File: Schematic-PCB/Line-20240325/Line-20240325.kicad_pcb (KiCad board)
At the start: 2 copper layers, 195 x 168 mm, 132 parts, among them J1 Conn_01x02_Pin, J2 Conn_01x04_Pin, J4 Conn_01x06_Pin, SW1 SW_Push, U34 ATmega2560-16A

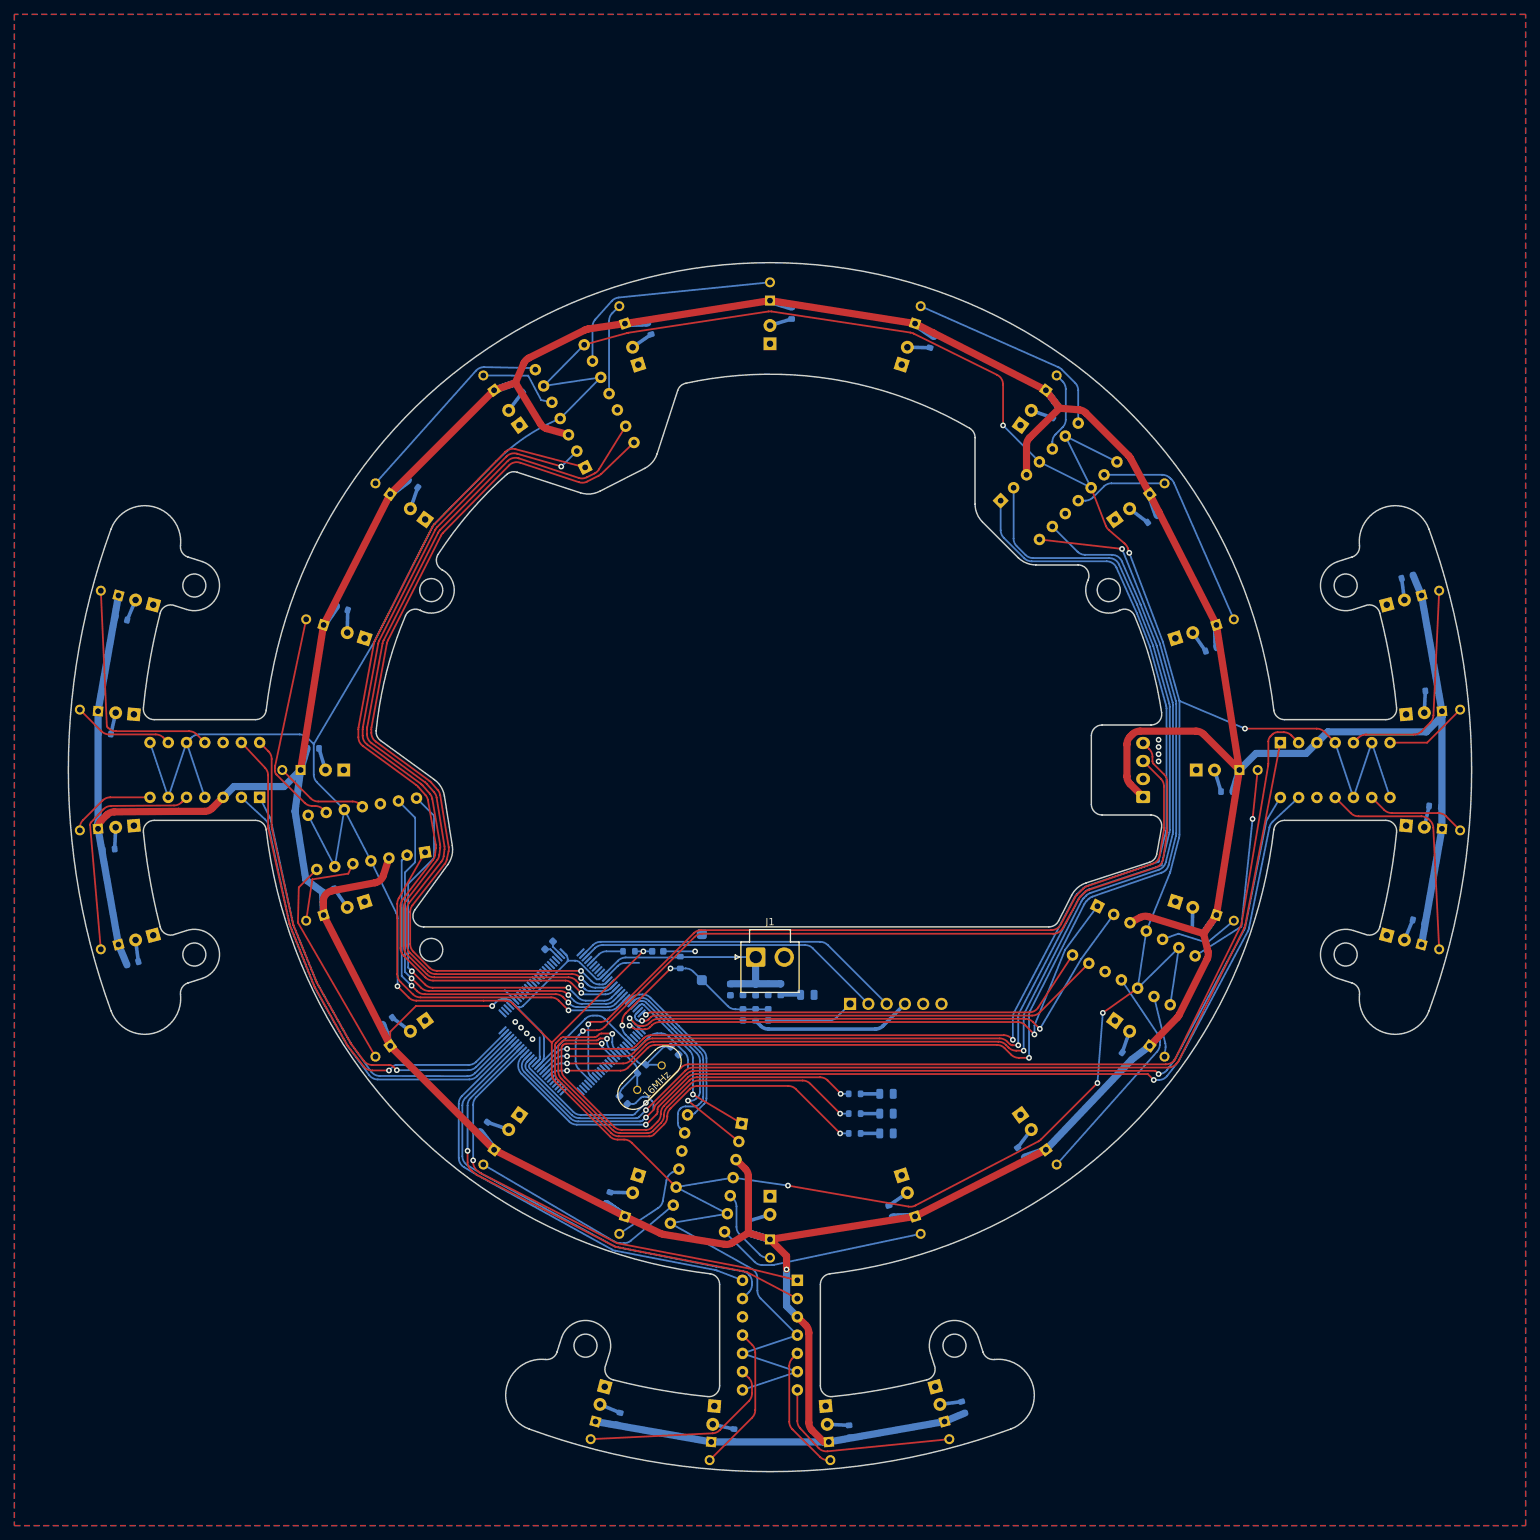
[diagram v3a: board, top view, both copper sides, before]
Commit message: ラインセンサ基板DR完了！！！！
発注用ファイルも出力完了、発注へ進みますー
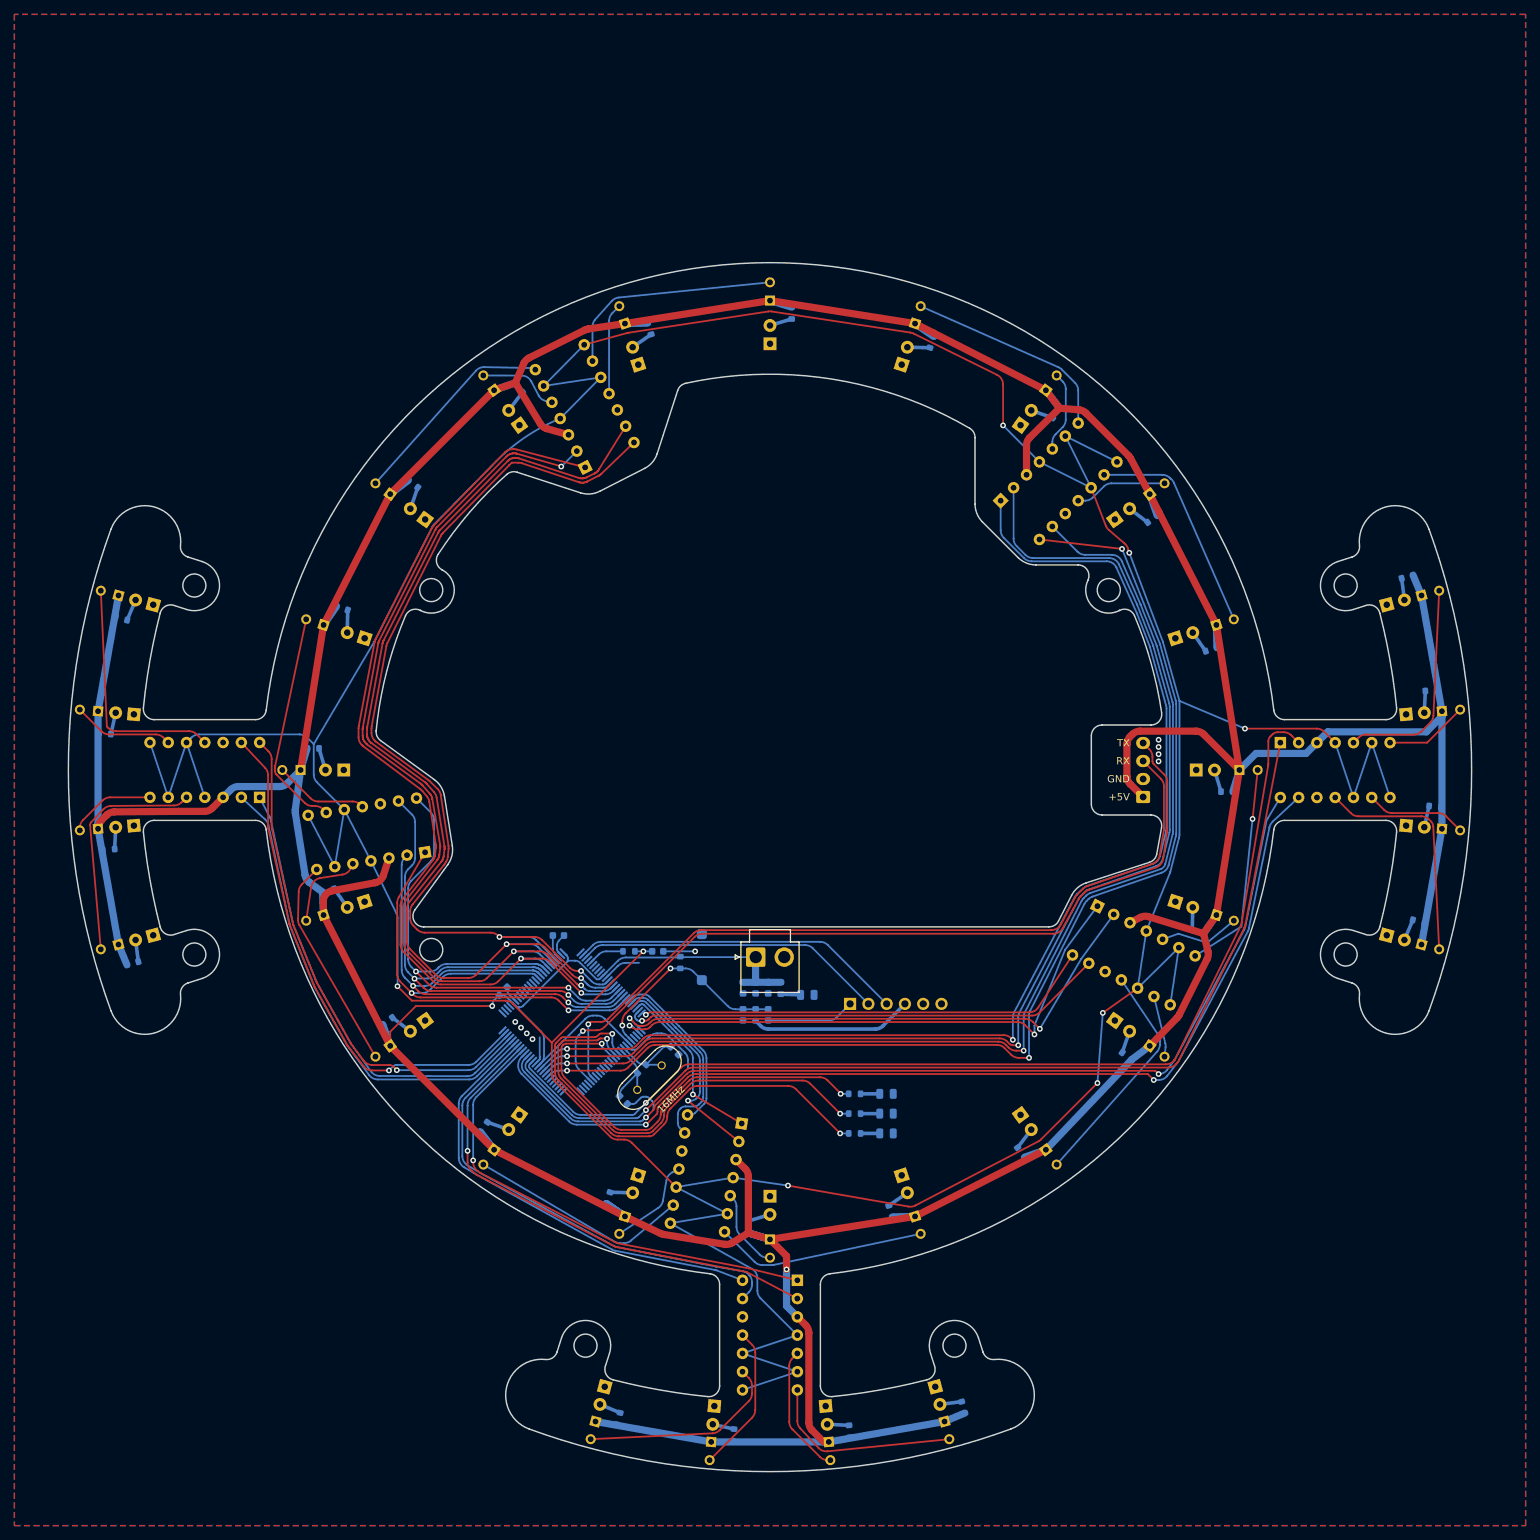
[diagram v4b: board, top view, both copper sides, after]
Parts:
- moved C4 31.6 mm to (-37.1, 30.7), turned to 45 degrees
- moved C6 1.89 mm to (-29.4, 23.0), turned to 0 degrees
- moved C2 0.25 mm to (-2.00, 30.3)
- moved C3 0.22 mm to (-3.75, 30.3)
- moved C1 0.22 mm to (-0.25, 30.3)
- moved R34 0.17 mm to (1.50, 30.3)
- renumbered C8 to 22pF, C7 to 22pF, 16MHz to Y1
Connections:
- U34 pad 90: unconnected-(U34-PF7/ADC7-Pad90) -> line08
- U34 pad 91: unconnected-(U34-PF6/ADC6-Pad91) -> line07
- U34 pad 92: unconnected-(U34-PF5/ADC5-Pad92) -> line06
- U34 pad 93: unconnected-(U34-PF4/ADC4-Pad93) -> line05
- U34 pad 94: unconnected-(U34-PF3/ADC3-Pad94) -> line04
- U34 pad 95: unconnected-(U34-PF2/ADC2-Pad95) -> line03
- U34 pad 96: unconnected-(U34-PF1/ADC1-Pad96) -> line02
- U34 pad 97: unconnected-(U34-PF0/ADC0-Pad97) -> line01
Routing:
- net line08: track 52.6 -> 71.7 mm, vias 1 -> 2
- net line07: track 50.2 -> 68.6 mm
- net line06: track 57.5 -> 75.7 mm
- net line05: track 57.6 -> 75.6 mm
- net line02: track 131.3 -> 142.3 mm, vias 1 -> 2
- net line03: track 123.6 -> 132.5 mm, vias 2 -> 3
- net line01: track 128.8 -> 135.7 mm, vias 1 -> 2
- net line04: track 126.0 -> 132.8 mm, vias 1 -> 2
- net +5V: track 915.7 -> 914.3 mm
- net GND: track 35.8 -> 36.9 mm
- net Net-(U34-AREF): track 2.34 -> 3.33 mm
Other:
- board text added: "+5V"
- board text added: "0.1µ"
- board text added: "10µ"
- board text added: "16MHz"
- board text added: "1K"
- board text added: "330"
- board text added: "D47"
- board text added: "D48"
- board text added: "D49"
- board text added: "GND"
- board text added: "LPF"
- board text added: "PWR"
- board text added: "RX"
- board text added: "TX"

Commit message: ラインセンサ基板のPCBをやり直してちょっと進めた
抵抗追加した分とかいろいろきれいにしてみる
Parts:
- removed 22pF (x2): 22pF, Capacitor_SMD:C_0603_1608Metric
- removed J4: Conn_01x06_Pin, Connector_PinSocket_2.54mm:PinSocket_1x06_P2.54mm_Horizontal
- removed U34: ATmega2560-16A, Package_QFP:TQFP-100_14x14mm_P0.5mm
- added C7: 22pF, Capacitor_SMD:C_0603_1608Metric, F.Cu at (199.9, 73.0)
- added C8: 0.1uF, Capacitor_SMD:C_0603_1608Metric, F.Cu at (199.9, 75.5)
- added J3: Conn_01x06_Pin, Connector_PinSocket_2.54mm:PinSocket_1x06_P2.54mm_Horizontal, B.Cu at (-27.8, 31.9)
- added R41: Line-Pulldown, Resistor_SMD:R_0603_1608Metric, B.Cu at (-35.3, 52.8)
- added R42: Line-Pulldown, Resistor_SMD:R_0603_1608Metric, B.Cu at (-17.2, 61.2)
- added R43: Line-Pulldown, Resistor_SMD:R_0603_1608Metric, B.Cu at (2.50, 63.5)
- added R44: Line-Pulldown, Resistor_SMD:R_0603_1608Metric, B.Cu at (22.0, 59.6)
- added R45: Line-Pulldown, Resistor_SMD:R_0603_1608Metric, B.Cu at (39.3, 49.9)
- added R46: Line-Pulldown, Resistor_SMD:R_0603_1608Metric, B.Cu at (52.8, 35.3)
- added R47: Line-Pulldown, Resistor_SMD:R_0603_1608Metric, B.Cu at (61.2, 17.2)
- added R48: Line-Pulldown, Resistor_SMD:R_0603_1608Metric, B.Cu at (63.5, -2.50)
- added R49: Line-Pulldown, Resistor_SMD:R_0603_1608Metric, B.Cu at (59.6, -22.0)
- added R50: Line-Pulldown, Resistor_SMD:R_0603_1608Metric, B.Cu at (49.9, -39.3)
- added R51: Line-Pulldown, Resistor_SMD:R_0603_1608Metric, B.Cu at (35.3, -52.8)
- added R52: Line-Pulldown, Resistor_SMD:R_0603_1608Metric, B.Cu at (17.2, -61.2)
- added R53: Line-Pulldown, Resistor_SMD:R_0603_1608Metric, F.Cu at (244.3, 54.5)
- added R54: Line-Pulldown, Resistor_SMD:R_0603_1608Metric, F.Cu at (244.3, 57.5)
- added R55: Line-Pulldown, Resistor_SMD:R_0603_1608Metric, F.Cu at (244.3, 60.5)
- added R56: Line-Pulldown, Resistor_SMD:R_0603_1608Metric, F.Cu at (244.3, 63.5)
- added R57: Line-Pulldown, Resistor_SMD:R_0603_1608Metric, F.Cu at (244.3, 66.5)
- added R58: Line-Pulldown, Resistor_SMD:R_0603_1608Metric, F.Cu at (244.3, 69.5)
- added R59: Line-Pulldown, Resistor_SMD:R_0603_1608Metric, F.Cu at (244.3, 72.5)
- added R60: Line-Pulldown, Resistor_SMD:R_0603_1608Metric, F.Cu at (244.3, 75.5)
- added R61: Line-Pulldown, Resistor_SMD:R_0603_1608Metric, F.Cu at (244.3, 78.5)
- added R62: Line-Pulldown, Resistor_SMD:R_0603_1608Metric, F.Cu at (244.3, 81.5)
- added R63: Line-Pulldown, Resistor_SMD:R_0603_1608Metric, F.Cu at (244.3, 84.5)
- added R64: Line-Pulldown, Resistor_SMD:R_0603_1608Metric, F.Cu at (244.3, 87.5)
- added R65: 330, Resistor_SMD:R_0603_1608Metric, F.Cu at (244.3, 90.5)
- added R66: 1M, Resistor_SMD:R_0603_1608Metric, F.Cu at (244.3, 93.5)
- added R67: 330, Resistor_SMD:R_0603_1608Metric, F.Cu at (244.3, 96.5)
- added R68: 10K, Resistor_SMD:R_0603_1608Metric, F.Cu at (244.3, 99.5)
- added R69: 330, Resistor_SMD:R_0603_1608Metric, F.Cu at (244.3, 102.5)
- added R70: 330, Resistor_SMD:R_0603_1608Metric, F.Cu at (244.3, 105.5)
- added R71: 10K, Resistor_SMD:R_0603_1608Metric, F.Cu at (244.3, 108.5)
- added R72: LPF, Resistor_SMD:R_0603_1608Metric, F.Cu at (244.3, 111.5)
- added REF**: MountingHole_3.2mm_M3, MountingHole:MountingHole_3.2mm_M3, F.Cu at (-80.0, -25.6)
- added REF**: MountingHole_3.2mm_M3, MountingHole:MountingHole_3.2mm_M3, F.Cu at (80.0, 25.6)
- added REF**: MountingHole_3.2mm_M3, MountingHole:MountingHole_3.2mm_M3, F.Cu at (-47.1, 25.0)
- added REF**: MountingHole_3.2mm_M3, MountingHole:MountingHole_3.2mm_M3, F.Cu at (47.1, -25.0)
- added REF**: MountingHole_3.2mm_M3, MountingHole:MountingHole_3.2mm_M3, F.Cu at (-80.0, 25.6)
- added REF**: MountingHole_3.2mm_M3, MountingHole:MountingHole_3.2mm_M3, F.Cu at (-47.1, -25.0)
- added REF**: MountingHole_3.2mm_M3, MountingHole:MountingHole_3.2mm_M3, F.Cu at (80.0, -25.6)
- added REF**: MountingHole_3.2mm_M3, MountingHole:MountingHole_3.2mm_M3, F.Cu at (-25.6, 80.0)
- added REF**: MountingHole_3.2mm_M3, MountingHole:MountingHole_3.2mm_M3, F.Cu at (25.6, 80.0)
- added U33: ATmega2560-16A, Package_QFP:TQFP-100_14x14mm_P0.5mm, B.Cu at (1.25, 36.2)
- C1, C2, C3, C4, Comp6, Comp7, Comp8, D21, D22, D23, D24, D25, D26, D27, D28, D29, D30, D31, D32, D33, D34, D35, D36, R21, R22, R23, R24, R25, R26, R27, R28, R29, R30, R31, R32, U21, U22, U23, U24, U25, U26, U27, U28, U29, U30, U31, U32: moved to F.Cu
- C10: value 10uF -> LPF; moved to F.Cu
- C5: value 22pF -> 0.1uF; moved to F.Cu
- C6, C9: value 0.1uF -> 22pF; moved to F.Cu
- J1: footprint @2024TOINOT2-Line:JST_VH_B2P-VH-B_1x02_P3.96mm_Vertical -> @2024TOINIOT2-Line:JST_VH_B2P-VH-B_1x02_P3.96mm_Vertical
- R33, R37: value 10K -> Line-Pulldown
- R34, R36, R38, R39: value 330 -> Line-Pulldown
- R35: value 1M -> Line-Pulldown
- R40: value 1K -> Line-Pulldown
- Y1: footprint @2024TOINOT2-Line:AL4BT -> @2024TOINIOT2-Line:AL4BT
- moved R21 337.8 mm to (236.8, 64.0), turned to 0 degrees
- moved R22 336.9 mm to (236.8, 66.5), turned to 0 degrees
- moved R23 333.8 mm to (236.8, 69.0), turned to 0 degrees
- moved R24 328.5 mm to (236.8, 71.5), turned to 0 degrees
- moved U21 299.6 mm to (184.8, 90.8), turned to 0 degrees
- moved U22 292.6 mm to (190.0, 59.3), turned to 0 degrees
- moved U23 290.2 mm to (190.0, 64.6), turned to 0 degrees
- moved Comp6 286.5 mm to (204.1, 47.0), turned to 0 degrees
- moved U24 285.4 mm to (190.0, 69.8), turned to 0 degrees
- moved D21 270.8 mm to (158.0, 92.1), turned to 0 degrees
- moved D22 261.9 mm to (163.5, 59.4), turned to 0 degrees
- moved D23 259.5 mm to (163.5, 64.9), turned to 0 degrees
- moved R25 258.4 mm to (236.8, 74.0), turned to 0 degrees
- moved D24 254.8 mm to (163.5, 70.3), turned to 0 degrees
- moved R26 242.4 mm to (236.8, 76.5), turned to 0 degrees
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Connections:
- C10 pad 1: line_threshold -> LineThreshold
- C5 pad 1: RESET -> GND
- C5 pad 2: GND -> Net-(U33-AREF)
- C6 pad 1: Net-(U34-AREF) -> GND
- C6 pad 2: GND -> Net-(U33-XTAL1)
- C9 pad 1: Net-(J4-Pin_1) -> RESET
- C9 pad 2: RESET -> GND
- Comp1 pad 1: line04 -> Line01
- Comp1 pad 10: line_threshold -> Raw4
- Comp1 pad 11: Net-(Comp1-4IN+) -> LineThreshold
- Comp1 pad 13: line02 -> Line04
- Comp1 pad 14: line01 -> Line03
- Comp1 pad 2: line03 -> Line02
- Comp1 pad 4: line_threshold -> LineThreshold
- Comp1 pad 5: Net-(Comp1-2IN+) -> Raw2
- Comp1 pad 6: line_threshold -> LineThreshold
- Comp1 pad 7: Net-(Comp1-1IN+) -> Raw1
- Comp1 pad 8: line_threshold -> LineThreshold
- Comp1 pad 9: Net-(Comp1-3IN+) -> Raw3
- Comp2 pad 1: line08 -> Line05
- Comp2 pad 10: line_threshold -> Raw8
- Comp2 pad 11: Net-(Comp2-4IN+) -> LineThreshold
- Comp2 pad 13: line06 -> Line08
- Comp2 pad 14: line05 -> Line07
- Comp2 pad 2: line07 -> Line06
- Comp2 pad 4: line_threshold -> LineThreshold
- Comp2 pad 5: Net-(Comp2-2IN+) -> Raw6
- Comp2 pad 6: line_threshold -> LineThreshold
- Comp2 pad 7: Net-(Comp2-1IN+) -> Raw5
- Comp2 pad 8: line_threshold -> LineThreshold
- Comp2 pad 9: Net-(Comp2-3IN+) -> Raw7
- Comp3 pad 1: line12 -> Line09
- Comp3 pad 10: line_threshold -> Raw12
- Comp3 pad 11: Net-(Comp3-4IN+) -> LineThreshold
- Comp3 pad 13: line10 -> Line12
- Comp3 pad 14: line09 -> Line11
- Comp3 pad 2: line11 -> Line10
- Comp3 pad 4: line_threshold -> LineThreshold
- Comp3 pad 5: Net-(Comp3-2IN+) -> Raw10
- Comp3 pad 6: line_threshold -> LineThreshold
- Comp3 pad 7: Net-(Comp3-1IN+) -> Raw9
- Comp3 pad 8: line_threshold -> LineThreshold
- Comp3 pad 9: Net-(Comp3-3IN+) -> Raw11
- Comp4 pad 1: line16 -> Line13
- Comp4 pad 10: line_threshold -> Raw16
- Comp4 pad 11: Net-(Comp4-4IN+) -> LineThreshold
- Comp4 pad 13: line13 -> Line16
- Comp4 pad 14: line14 -> Line15
- Comp4 pad 2: line15 -> Line14
- Comp4 pad 4: line_threshold -> LineThreshold
- Comp4 pad 5: Net-(Comp4-2IN+) -> Raw14
- Comp4 pad 6: line_threshold -> LineThreshold
- Comp4 pad 7: Net-(Comp4-1IN+) -> Raw13
- Comp4 pad 8: line_threshold -> LineThreshold
- Comp4 pad 9: Net-(Comp4-3IN+) -> Raw15
- Comp5 pad 1: line20 -> Line17
- Comp5 pad 10: line_threshold -> Raw20
- Comp5 pad 11: Net-(Comp5-4IN+) -> LineThreshold
- Comp5 pad 13: line18 -> Line20
- Comp5 pad 14: line17 -> Line19
- Comp5 pad 2: line19 -> Line18
- Comp5 pad 4: line_threshold -> LineThreshold
- Comp5 pad 5: Net-(Comp5-2IN+) -> Raw18
- Comp5 pad 6: line_threshold -> LineThreshold
- Comp5 pad 7: Net-(Comp5-1IN+) -> Raw17
- Comp5 pad 8: line_threshold -> LineThreshold
- Comp5 pad 9: Net-(Comp5-3IN+) -> Raw19
- Comp6 pad 1: line23 -> Line21
- Comp6 pad 10: line_threshold -> Raw24
- Comp6 pad 11: Net-(Comp6-4IN+) -> LineThreshold
- Comp6 pad 13: line21 -> Line24
- Comp6 pad 14: line22 -> Line23
- Comp6 pad 2: line24 -> Line22
- Comp6 pad 4: line_threshold -> LineThreshold
- Comp6 pad 5: Net-(Comp6-2IN+) -> Raw22
- Comp6 pad 6: line_threshold -> LineThreshold
- Comp6 pad 7: Net-(Comp6-1IN+) -> Raw21
- Comp6 pad 8: line_threshold -> LineThreshold
- Comp6 pad 9: Net-(Comp6-3IN+) -> Raw23
- Comp7 pad 1: line28 -> Line25
- Comp7 pad 10: line_threshold -> Raw28
- Comp7 pad 11: Net-(Comp7-4IN+) -> LineThreshold
- Comp7 pad 13: line26 -> Line28
- Comp7 pad 14: line25 -> Line27
- Comp7 pad 2: line27 -> Line26
- Comp7 pad 4: line_threshold -> LineThreshold
- Comp7 pad 5: Net-(Comp7-2IN+) -> Raw26
- Comp7 pad 6: line_threshold -> LineThreshold
- Comp7 pad 7: Net-(Comp7-1IN+) -> Raw25
- Comp7 pad 8: line_threshold -> LineThreshold
- Comp7 pad 9: Net-(Comp7-3IN+) -> Raw27
- Comp8 pad 1: line31 -> Line29
- Comp8 pad 10: line_threshold -> Raw32
- Comp8 pad 11: Net-(Comp8-4IN+) -> LineThreshold
- Comp8 pad 13: line29 -> Line32
- Comp8 pad 14: line30 -> Line31
- Comp8 pad 2: line32 -> Line30
- Comp8 pad 4: line_threshold -> LineThreshold
- Comp8 pad 5: Net-(Comp8-2IN+) -> Raw30
- Comp8 pad 6: line_threshold -> LineThreshold
- Comp8 pad 7: Net-(Comp8-1IN+) -> Raw29
- Comp8 pad 8: line_threshold -> LineThreshold
- Comp8 pad 9: Net-(Comp8-3IN+) -> Raw31
- R33 pad 1: +5V -> Raw1
- R33 pad 2: RESET -> GND
- R34 pad 1: +5V -> Raw2
- R34 pad 2: Net-(D33-A) -> GND
- R35 pad 1: Net-(U34-XTAL2) -> Raw3
- R35 pad 2: Net-(U34-XTAL1) -> GND
- R36 pad 1: Net-(D34-A) -> Raw4
- R36 pad 2: Net-(U34-PL2/D47) -> GND
- R37 pad 1: VBUS -> Raw5
- R37 pad 2: RESET -> GND
- R38 pad 1: Net-(D35-A) -> Raw6
- R38 pad 2: Net-(U34-PL1/D48) -> GND
- R39 pad 1: Net-(D36-A) -> Raw7
- R39 pad 2: Net-(U34-PL0/D49) -> GND
- R40 pad 1: Net-(U34-PE3/D5) -> Raw8
- R40 pad 2: line_threshold -> GND
- U1 pad 1: Net-(Comp1-3IN+) -> Raw1
- U10 pad 1: Net-(Comp3-4IN+) -> Raw10
- U11 pad 1: Net-(Comp3-2IN+) -> Raw11
- U12 pad 1: Net-(Comp3-1IN+) -> Raw12
- U13 pad 1: Net-(Comp4-4IN+) -> Raw13
- U14 pad 1: Net-(Comp4-3IN+) -> Raw14
- U15 pad 1: Net-(Comp4-2IN+) -> Raw15
- U16 pad 1: Net-(Comp4-1IN+) -> Raw16
- U17 pad 1: Net-(Comp5-3IN+) -> Raw17
- U18 pad 1: Net-(Comp5-4IN+) -> Raw18
- U19 pad 1: Net-(Comp5-2IN+) -> Raw19
- U2 pad 1: Net-(Comp1-4IN+) -> Raw2
- U20 pad 1: Net-(Comp5-1IN+) -> Raw20
- U21 pad 1: Net-(Comp6-4IN+) -> Raw21
- U22 pad 1: Net-(Comp6-3IN+) -> Raw22
- U23 pad 1: Net-(Comp6-1IN+) -> Raw23
- U24 pad 1: Net-(Comp6-2IN+) -> Raw24
- U25 pad 1: Net-(Comp7-3IN+) -> Raw25
- U26 pad 1: Net-(Comp7-4IN+) -> Raw26
- U27 pad 1: Net-(Comp7-2IN+) -> Raw27
- U28 pad 1: Net-(Comp7-1IN+) -> Raw28
- U29 pad 1: Net-(Comp8-4IN+) -> Raw29
- U3 pad 1: Net-(Comp1-2IN+) -> Raw3
- U30 pad 1: Net-(Comp8-3IN+) -> Raw30
- U31 pad 1: Net-(Comp8-1IN+) -> Raw31
- U32 pad 1: Net-(Comp8-2IN+) -> Raw32
- U4 pad 1: Net-(Comp1-1IN+) -> Raw4
- U5 pad 1: Net-(Comp2-3IN+) -> Raw5
- U6 pad 1: Net-(Comp2-4IN+) -> Raw6
- U7 pad 1: Net-(Comp2-2IN+) -> Raw7
- U8 pad 1: Net-(Comp2-1IN+) -> Raw8
- U9 pad 1: Net-(Comp3-3IN+) -> Raw9
- Y1 pad 1: Net-(U34-XTAL2) -> Net-(U33-XTAL2)
- Y1 pad 2: Net-(U34-XTAL1) -> Net-(U33-XTAL1)
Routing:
- net +5V: track 914.3 -> 60.5 mm, vias 2 -> 0
- net line_threshold: track 630.7 -> 0.00 mm, vias 8 -> 0
- net line19: track 169.3 -> 0.00 mm, vias 2 -> 0
- net line20: track 166.9 -> 0.00 mm, vias 2 -> 0
- net line17: track 162.3 -> 0.00 mm, vias 3 -> 0
- net line18: track 159.1 -> 0.00 mm, vias 2 -> 0
- net line32: track 148.6 -> 0.00 mm, vias 1 -> 0
- net line31: track 145.2 -> 0.00 mm, vias 1 -> 0
- net line29: track 143.3 -> 0.00 mm, vias 2 -> 0
- net line02: track 142.3 -> 0.00 mm, vias 2 -> 0
- net line30: track 139.5 -> 0.00 mm, vias 2 -> 0
- net line01: track 135.7 -> 0.00 mm, vias 2 -> 0
- net line04: track 132.8 -> 0.00 mm, vias 2 -> 0
- net line03: track 132.5 -> 0.00 mm, vias 3 -> 0
- net Line-MD-Main=RX_5V: track 115.9 -> 0.00 mm, vias 1 -> 0
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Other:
- outline, holes or cut-outs redrawn
- board text removed: "+5V"
- board text removed: "0.1µ"
- board text removed: "10µ"
- board text removed: "16MHz"
- board text removed: "1K"
- board text removed: "330"
- board text removed: "D47"
- board text removed: "D48"
- board text removed: "D49"
- board text removed: "GND"
- board text removed: "LPF"
- board text removed: "PWR"
- board text removed: "RX"
- board text removed: "TX"

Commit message: ラインセンサ基板の配線を進めた
キッツイワー
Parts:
- C6, C7, Comp6, Comp7, Comp8, D21, D22, D23, D24, D25, D26, D27, D28, D29, D30, D31, D32, R21, R22, R23, R24, R25, R26, R27, R28, R29, R30, R31, R32, R53, R54, R55, R56, R57, R58, R59, R60, R61, R62, R63, R64, R66, U21, U22, U23, U24, U25, U26, U27, U28, U29, U30, U31, U32, Y1: moved to B.Cu
- moved R53 342.8 mm to (-90.1, -20.8), turned to 167 degrees
- moved R54 342.4 mm to (-92.4, -4.84), turned to 177 degrees
- moved R55 339.7 mm to (-91.8, 11.3), turned to -173 degrees
- moved R21 337.8 mm to (-88.5, -27.0), turned to -17 degrees
- moved R22 337.7 mm to (-91.8, -11.3), turned to -7 degrees
- moved R23 335.4 mm to (-92.4, 4.84), turned to 3 degrees
- moved R56 334.8 mm to (-88.5, 27.0), turned to -163 degrees
- moved R24 330.9 mm to (-90.1, 20.8), turned to 13 degrees
- moved U21 294.7 mm to (-86.9, -23.3), turned to 165 degrees
- moved U22 287.6 mm to (-89.7, -7.84), turned to 175 degrees
- moved Comp6 286.5 mm to (-78.5, 0.00), turned to -90 degrees
- moved U23 285.4 mm to (-89.7, 7.84), turned to -175 degrees
- moved U24 280.8 mm to (-86.9, 23.3), turned to -165 degrees
- moved D21 275.7 mm to (-91.8, -24.6), turned to -15 degrees
- moved D22 266.8 mm to (-94.6, -8.28), turned to -5 degrees
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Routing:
- net +5V: track 60.5 -> 765.9 mm
- net Line04: track 17.9 -> 161.9 mm
- net Line03: track 17.0 -> 160.2 mm
- net Line02: track 16.3 -> 150.0 mm
- net Line01: track 15.7 -> 148.9 mm
- net Line08: track 23.5 -> 91.6 mm
- net Line07: track 20.3 -> 88.1 mm
- net Line05: track 18.8 -> 78.6 mm
- net Line06: track 19.7 -> 78.8 mm
- net RX-USB: track 0.00 -> 37.8 mm, vias 0 -> 1
- net Line12: track 41.4 -> 6.11 mm
- net TX-USB: track 0.00 -> 33.9 mm, vias 0 -> 1
- net Raw8: track 4.26 -> 37.4 mm
- net Raw13: track 4.26 -> 35.9 mm
- net Raw4: track 4.26 -> 35.8 mm
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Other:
- board text added: "16MHz"

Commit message: フットプリントを修正した
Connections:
- J3 pad 4: VBUS -> unconnected-(J3-Pin_4-Pad4)
- R68 pad 1: VBUS -> +5V
